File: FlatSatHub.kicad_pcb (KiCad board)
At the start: 2 copper layers, 129.3 x 129.3 mm, 24 parts, among them J1 DB26_Male_HighDensity_Mountin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, J10 Conn_02x02_Odd_Even, J11 DB26_Male_HighDensity_Mountin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, J12 Conn_02x02_Odd_Even, J13 DB26_Male_HighDensity_Mountin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, J14 Conn_02x02_Odd_Even, J15 DB26_Male_HighDensity_Mountin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, J16 Conn_02x02_Odd_Even, J2 Conn_02x02_Odd_Even, J3 DB26_Male_HighDensity_Mountin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, J4 Conn_02x02_Odd_Even, J5 DB26_Male_HighDensity_Mountin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, J6 Conn_02x02_Odd_Even, J7 DB26_Male_HighDensity_Mountin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, J8 Conn_02x02_Odd_Even, J9 DB26_Male_HighDensity_Mountin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, SW1 SW_SPST, SW2 SW_SPST, SW3 SW_SPST, SW4 SW_SPST, SW5 SW_SPST, SW6 SW_SPST, SW7 SW_SPST, SW8 SW_SPST

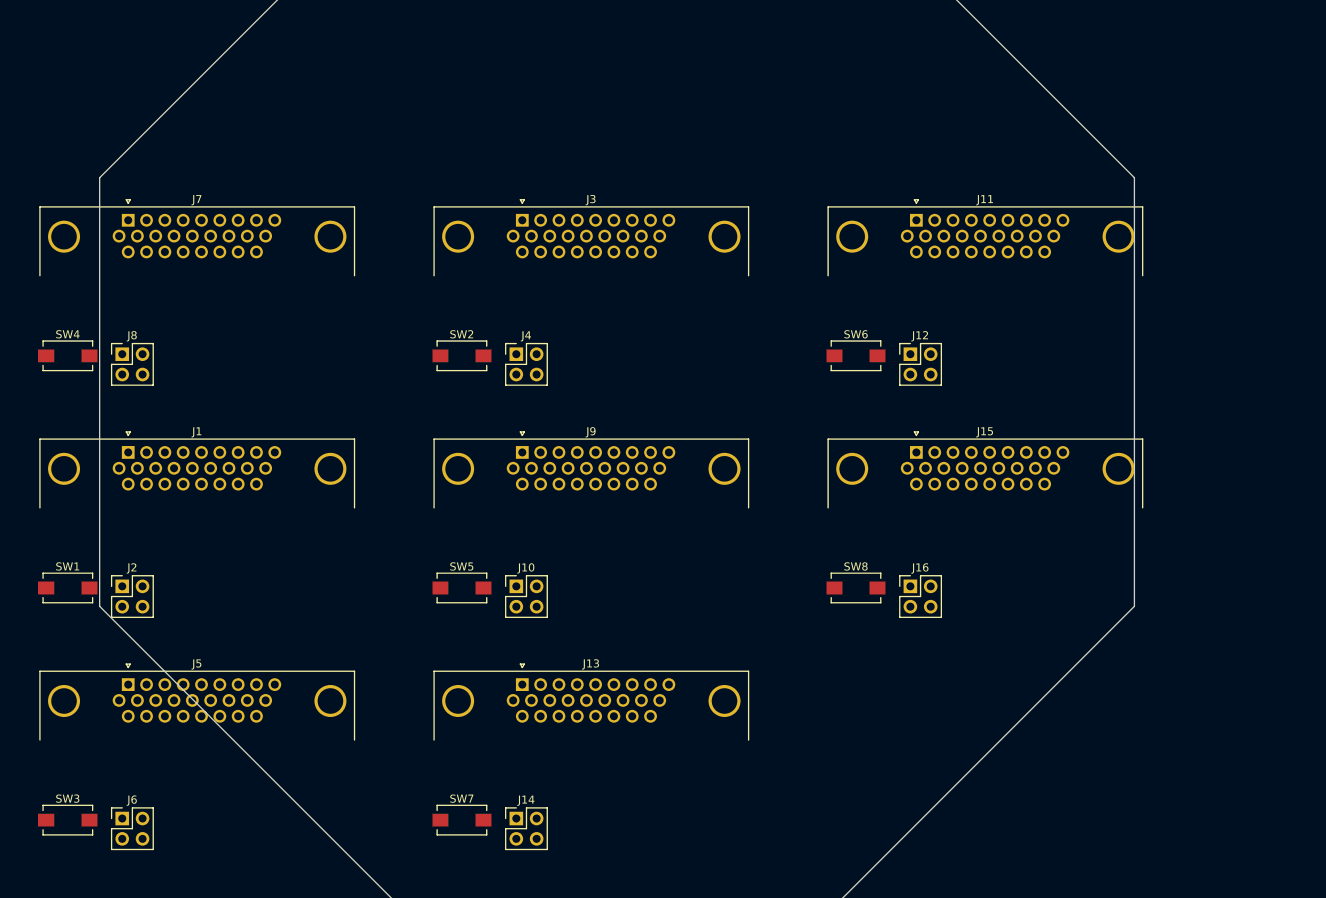
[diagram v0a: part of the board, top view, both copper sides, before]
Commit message: create footprints
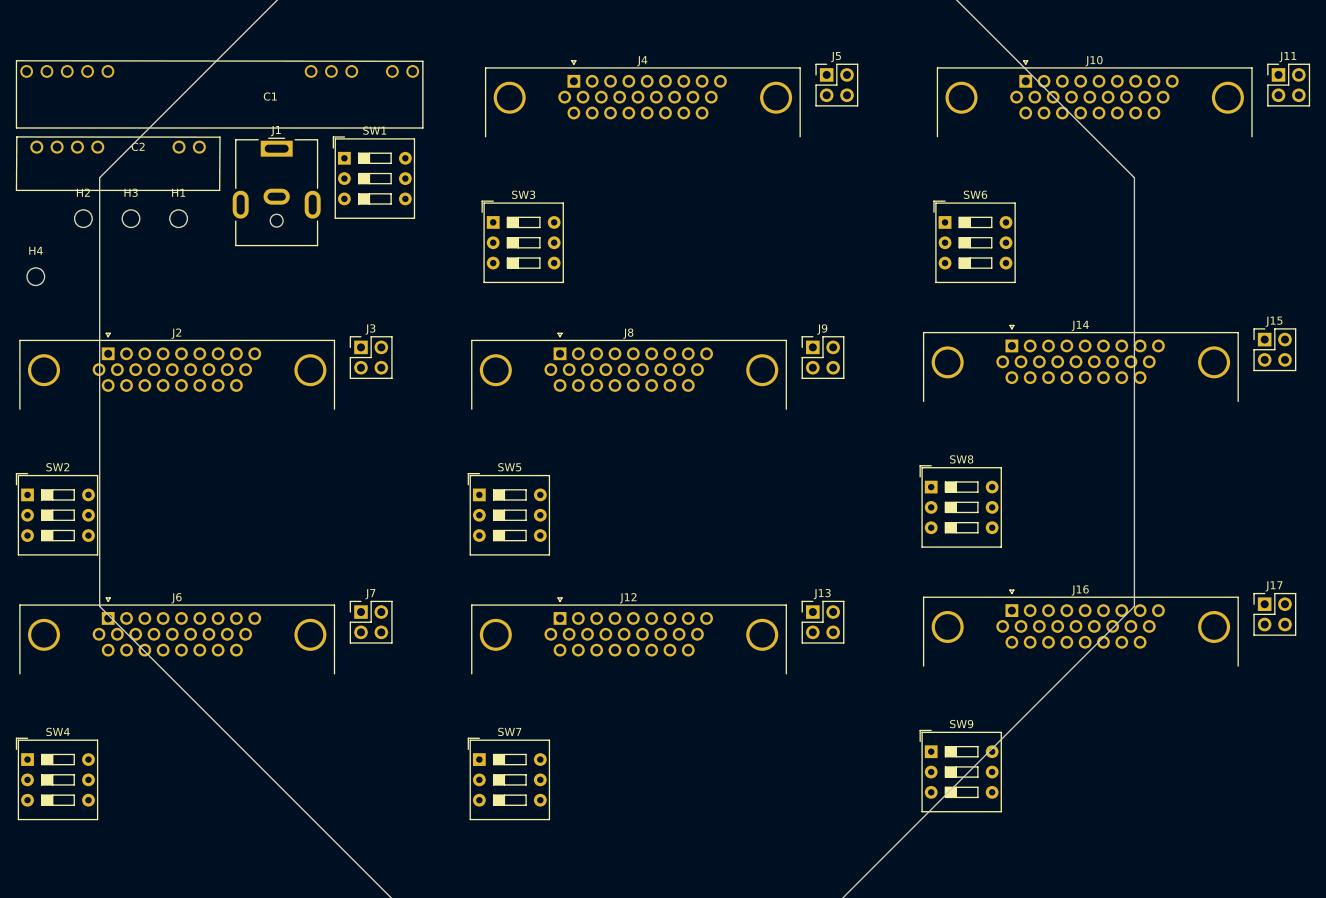
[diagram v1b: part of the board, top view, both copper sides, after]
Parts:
- added C1: CINCON-SIPSMT10-12, FlatSatHub:CINCON-SIPSMT10-12, F.Cu at (106.7, 34.9)
- added C2: bel-xRBA-06E2Ax, FlatSatHub:BEL-xRBA-06E2Ax, F.Cu at (87.6, 45.0)
- added H1: MountingHole_Pad, MountingHole:MountingHole_2.2mm_M2, F.Cu at (95.2, 53.3)
- added H2: MountingHole_Pad, MountingHole:MountingHole_2.2mm_M2, F.Cu at (83.3, 53.3)
- added H3: MountingHole_Pad, MountingHole:MountingHole_2.2mm_M2, F.Cu at (89.2, 53.3)
- added H4: MountingHole_Pad, MountingHole:MountingHole_2.2mm_M2, F.Cu at (77.3, 60.6)
- added J17: Conn_02x02_Odd_Even, Connector_PinHeader_2.54mm:PinHeader_2x02_P2.54mm_Vertical, F.Cu at (231.0, 101.5)
- added SW9: SW_DIP_x03, Button_Switch_THT:SW_DIP_SPSTx03_Slide_9.78x9.8mm_W7.62mm_P2.54mm, F.Cu at (189.3, 120.0)
- J1: value DB26_Male_HighDensity_MountingHoles -> Jack-DC; footprint Connector_Dsub:DSUB-26-HD_Male_Horizontal_P2.29x1.98mm_EdgePinOffset3.03mm_Housed_MountingHolesOffset4.94mm -> Connector_BarrelJack:BarrelJack_CUI_PJ-063AH_Horizontal
- J10, J12, J14, J16, J2, J4, J6, J8: value Conn_02x02_Odd_Even -> DB26_Male_HighDensity_MountingHoles; footprint Connector_PinHeader_2.54mm:PinHeader_2x02_P2.54mm_Vertical -> Connector_Dsub:DSUB-26-HD_Male_Horizontal_P2.29x1.98mm_EdgePinOffset3.03mm_Housed_MountingHolesOffset4.94mm
- J11, J13, J15, J3, J5, J7, J9: value DB26_Male_HighDensity_MountingHoles -> Conn_02x02_Odd_Even; footprint Connector_Dsub:DSUB-26-HD_Male_Horizontal_P2.29x1.98mm_EdgePinOffset3.03mm_Housed_MountingHolesOffset4.94mm -> Connector_PinHeader_2.54mm:PinHeader_2x02_P2.54mm_Vertical
- SW1, SW2, SW3, SW4, SW5, SW6, SW7, SW8: value SW_SPST -> SW_DIP_x03; footprint Button_Switch_SMD:SW_SPST_EVQPE1 -> Button_Switch_THT:SW_DIP_SPSTx03_Slide_9.78x9.8mm_W7.62mm_P2.54mm
- moved J5 115.9 mm to (176.2, 35.4)
- moved SW3 91.7 mm to (134.5, 53.8)
- moved J10 89.7 mm to (201.1, 36.2)
- moved J14 85.6 mm to (199.4, 69.2)
- moved SW1 63.9 mm to (115.9, 45.8)
- moved SW2 57.0 mm to (76.3, 87.9)
- moved J7 57.0 mm to (118.0, 102.5)
- moved J12 54.9 mm to (142.9, 103.3)
- moved J8 54.7 mm to (142.9, 70.2)
- moved SW4 50.7 mm to (76.3, 120.9)
- moved J11 48.8 mm to (232.7, 35.4)
- moved J15 45.8 mm to (231.0, 68.4)
- moved J1 42.3 mm to (107.5, 44.6)
- moved J9 38.6 mm to (174.5, 69.4)
- moved J13 37.4 mm to (174.5, 102.5)
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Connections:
- J1 pad 1: /sheet5F162098/I2C2_SDA -> /VBat
- J1 pad 2: /SPI1_MISO -> GND
- J10 pad 1: /sheet5F164939/UART2_TX -> I2C2_SDA
- J10 pad 2: /sheet5F164939/UART2_RX -> SPI1_MISO
- J10 pad 3: /sheet5F164939/UART1_TX -> SPI1_SS
- J10 pad 4: /sheet5F164939/UART1_RX -> SPI4_SS
- J11 pad 1: /sheet5F16493A/I2C2_SDA -> /sheet5F112855/sheet5F10EEC4/UART2_TX
- J11 pad 2: /SPI1_MISO -> /sheet5F112855/sheet5F10EEC4/UART2_RX
- J11 pad 3: /SPI1_SS -> /sheet5F112855/sheet5F10EEC4/UART1_TX
- J11 pad 4: /SPI4_SS -> /sheet5F112855/sheet5F10EEC4/UART1_RX
- J12 pad 1: /sheet5F16493A/UART2_TX -> I2C2_SDA
- J12 pad 2: /sheet5F16493A/UART2_RX -> SPI1_MISO
- J12 pad 3: /sheet5F16493A/UART1_TX -> SPI1_SS
- J12 pad 4: /sheet5F16493A/UART1_RX -> SPI4_SS
- J13 pad 1: /sheet5F16493B/I2C2_SDA -> /sheet5F112856/sheet5F10EEC4/UART2_TX
- J13 pad 2: /SPI1_MISO -> /sheet5F112856/sheet5F10EEC4/UART2_RX
- J13 pad 3: /SPI1_SS -> /sheet5F112856/sheet5F10EEC4/UART1_TX
- J13 pad 4: /SPI4_SS -> /sheet5F112856/sheet5F10EEC4/UART1_RX
- J14 pad 1: /sheet5F16493B/UART2_TX -> I2C2_SDA
- J14 pad 2: /sheet5F16493B/UART2_RX -> SPI1_MISO
- J14 pad 3: /sheet5F16493B/UART1_TX -> SPI1_SS
- J14 pad 4: /sheet5F16493B/UART1_RX -> SPI4_SS
- J15 pad 1: /sheet5F16493C/I2C2_SDA -> /sheet5F112857/sheet5F10EEC4/UART2_TX
- J15 pad 2: /SPI1_MISO -> /sheet5F112857/sheet5F10EEC4/UART2_RX
- J15 pad 3: /SPI1_SS -> /sheet5F112857/sheet5F10EEC4/UART1_TX
- J15 pad 4: /SPI4_SS -> /sheet5F112857/sheet5F10EEC4/UART1_RX
- J16 pad 1: /sheet5F16493C/UART2_TX -> I2C2_SDA
- J16 pad 2: /sheet5F16493C/UART2_RX -> SPI1_MISO
- J16 pad 3: /sheet5F16493C/UART1_TX -> SPI1_SS
- J16 pad 4: /sheet5F16493C/UART1_RX -> SPI4_SS
- J2 pad 1: /sheet5F162098/UART2_TX -> I2C2_SDA
- J2 pad 2: /sheet5F162098/UART2_RX -> SPI1_MISO
- J2 pad 3: /sheet5F162098/UART1_TX -> SPI1_SS
- J2 pad 4: /sheet5F162098/UART1_RX -> SPI4_SS
- J3 pad 1: /sheet5F162B0B/I2C2_SDA -> /Sheet5F10DACD/sheet5F10EEC4/UART2_TX
- J3 pad 2: /SPI1_MISO -> /Sheet5F10DACD/sheet5F10EEC4/UART2_RX
- J3 pad 3: /SPI1_SS -> /Sheet5F10DACD/sheet5F10EEC4/UART1_TX
- J3 pad 4: /SPI4_SS -> /Sheet5F10DACD/sheet5F10EEC4/UART1_RX
- J4 pad 1: /sheet5F162B0B/UART2_TX -> I2C2_SDA
- J4 pad 2: /sheet5F162B0B/UART2_RX -> SPI1_MISO
- J4 pad 3: /sheet5F162B0B/UART1_TX -> SPI1_SS
- J4 pad 4: /sheet5F162B0B/UART1_RX -> SPI4_SS
- J5 pad 1: /sheet5F162B0C/I2C2_SDA -> /sheet5F1123F7/sheet5F10EEC4/UART2_TX
- J5 pad 2: /SPI1_MISO -> /sheet5F1123F7/sheet5F10EEC4/UART2_RX
- J5 pad 3: /SPI1_SS -> /sheet5F1123F7/sheet5F10EEC4/UART1_TX
- J5 pad 4: /SPI4_SS -> /sheet5F1123F7/sheet5F10EEC4/UART1_RX
- J6 pad 1: /sheet5F162B0C/UART2_TX -> I2C2_SDA
- J6 pad 2: /sheet5F162B0C/UART2_RX -> SPI1_MISO
- J6 pad 3: /sheet5F162B0C/UART1_TX -> SPI1_SS
- J6 pad 4: /sheet5F162B0C/UART1_RX -> SPI4_SS
- J7 pad 1: /sheet5F15D03F/I2C2_SDA -> /sheet5F112649/sheet5F10EEC4/UART2_TX
- J7 pad 2: /SPI1_MISO -> /sheet5F112649/sheet5F10EEC4/UART2_RX
- J7 pad 3: /SPI1_SS -> /sheet5F112649/sheet5F10EEC4/UART1_TX
- J7 pad 4: /SPI4_SS -> /sheet5F112649/sheet5F10EEC4/UART1_RX
- J8 pad 1: /sheet5F15D03F/UART2_TX -> I2C2_SDA
- J8 pad 2: /sheet5F15D03F/UART2_RX -> SPI1_MISO
- J8 pad 3: /sheet5F15D03F/UART1_TX -> SPI1_SS
- J8 pad 4: /sheet5F15D03F/UART1_RX -> SPI4_SS
- J9 pad 1: /sheet5F164939/I2C2_SDA -> /sheet5F11264A/sheet5F10EEC4/UART2_TX
- J9 pad 2: /SPI1_MISO -> /sheet5F11264A/sheet5F10EEC4/UART2_RX
- J9 pad 3: /SPI1_SS -> /sheet5F11264A/sheet5F10EEC4/UART1_TX
- J9 pad 4: /SPI4_SS -> /sheet5F11264A/sheet5F10EEC4/UART1_RX
- SW1 pad 1: /VCC -> /VBat
- SW1 pad 2: /VCC -> /VBat
- SW2 pad 1: /VCC -> VCC
- SW2 pad 2: /VCC -> /Sheet5F10DACD/sheet5F10EEC4/3V3
- SW3 pad 1: /VCC -> VCC
- SW3 pad 2: /VCC -> /sheet5F1123F7/sheet5F10EEC4/3V3
- SW4 pad 1: /VCC -> VCC
- SW4 pad 2: /VCC -> /sheet5F112649/sheet5F10EEC4/3V3
- SW5 pad 1: /VCC -> VCC
- SW5 pad 2: /VCC -> /sheet5F11264A/sheet5F10EEC4/3V3
- SW6 pad 1: /VCC -> VCC
- SW6 pad 2: /VCC -> /sheet5F112855/sheet5F10EEC4/3V3
- SW7 pad 1: /VCC -> VCC
- SW7 pad 2: /VCC -> /sheet5F112856/sheet5F10EEC4/3V3
- SW8 pad 1: /VCC -> VCC
- SW8 pad 2: /VCC -> /sheet5F112857/sheet5F10EEC4/3V3

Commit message: First placement and autorouting
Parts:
- C1: value CINCON-SIPSMT10-12 -> SIPSMT10-12
- H1, H2, H3, H4: footprint MountingHole:MountingHole_2.2mm_M2 -> MountingHole:MountingHole_2.2mm_M2_Pad
- J10, J12, J14, J16, J2, J4, J6, J8: footprint Connector_Dsub:DSUB-26-HD_Male_Horizontal_P2.29x1.98mm_EdgePinOffset3.03mm_Housed_MountingHolesOffset4.94mm -> Connector_Dsub:DSUB-26-HD_Female_Horizontal_P2.29x1.98mm_EdgePinOffset8.35mm_Housed_MountingHolesOffset10.89mm
- moved H2 95.3 mm to (154.9, 116.2)
- moved H3 80.3 mm to (161.3, 88.9)
- moved J11 74.5 mm to (163.2, 62.2), turned to 135 degrees
- moved J9 71.2 mm to (103.5, 63.5), turned to 225 degrees
- moved C2 70.4 mm to (144.1, 87.0), turned to 270 degrees
- moved J1 68.7 mm to (134.0, 108.0), turned to 90 degrees
- moved J17 67.8 mm to (165.2, 118.2), turned to 45 degrees
- moved J15 60.2 mm to (174.6, 89.5), turned to 90 degrees
- moved J13 52.8 mm to (132.1, 134.0)
- moved J8 52.3 mm to (91.4, 61.0), turned to 225 degrees
- moved C1 49.6 mm to (120.7, 82.5), turned to 90 degrees
- moved J5 46.9 mm to (131.4, 49.5), turned to 180 degrees
- moved H4 43.0 mm to (108.6, 90.2)
- moved J12 40.2 mm to (142.9, 143.5)
- moved J10 39.0 mm to (163.8, 47.6), turned to 135 degrees
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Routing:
- net SPI4_MOSI: track 0.00 -> 397.0 mm, vias 0 -> 3
- net SPI4_MISO: track 0.00 -> 388.1 mm, vias 0 -> 4
- net SPI1_SS: track 0.00 -> 363.7 mm, vias 0 -> 4
- net SPI1_SCK: track 0.00 -> 360.9 mm, vias 0 -> 3
- net SPI4_SCK: track 0.00 -> 351.2 mm, vias 0 -> 5
- net CAN1_RX: track 0.00 -> 345.4 mm, vias 0 -> 4
- net I2C2_SCL: track 0.00 -> 343.6 mm, vias 0 -> 3
- net I2C1_SCL: track 0.00 -> 343.6 mm, vias 0 -> 3
- net I2C1_SDA: track 0.00 -> 342.3 mm, vias 0 -> 5
- net SPI1_MOSI: track 0.00 -> 340.0 mm, vias 0 -> 3
- net I2C2_SDA: track 0.00 -> 313.1 mm, vias 0 -> 4
- net CAN1_TX: track 0.00 -> 307.1 mm, vias 0 -> 4
- net SPI4_SS: track 0.00 -> 307.0 mm, vias 0 -> 3
- net SPI1_MISO: track 0.00 -> 306.8 mm, vias 0 -> 4
- net GND: track 0.00 -> 70.7 mm, vias 0 -> 3
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- added copper zone on In2.Cu, net /3V3
- added copper zone on B.Cu, net /5V
- added copper zone on F.Cu, net GND
- added copper zone on In1.Cu, net VCC
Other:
- copper layers 2 -> 4
- rule trace_min: 0.2 -> 0.15

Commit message: rework power management schematic
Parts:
- added R1: R, Resistor_SMD:R_0603_1608Metric_Pad1.05x0.95mm_HandSolder, F.Cu at (135.3, 101.0)
- added R2: R, Resistor_SMD:R_0603_1608Metric_Pad1.05x0.95mm_HandSolder, F.Cu at (137.8, 94.6)
- C1: value SIPSMT10-12 -> CINCON-SIPSMT10-12
- J10, J12, J14, J16, J2, J4, J6, J8: footprint Connector_Dsub:DSUB-26-HD_Female_Horizontal_P2.29x1.98mm_EdgePinOffset8.35mm_Housed_MountingHolesOffset10.89mm -> Connector_Dsub:DSUB-26-HD_Male_Horizontal_P2.29x1.98mm_EdgePinOffset3.03mm_Housed_MountingHolesOffset4.94mm
- moved J13 263.3 mm to (371.3, 24.0)
- moved J7 230.0 mm to (314.8, 24.0), turned to 0 degrees
- moved J12 229.8 mm to (339.7, 24.8)
- moved J17 214.9 mm to (371.3, 57.0), turned to 0 degrees
- moved J6 210.3 mm to (283.2, 24.8), turned to 0 degrees
- moved SW7 210.0 mm to (329.6, 42.4)
- moved SW4 187.7 mm to (273.1, 42.4), turned to 0 degrees
- moved SW9 181.1 mm to (329.6, 75.5), turned to 0 degrees
- moved J3 179.6 mm to (258.3, 24.0), turned to 0 degrees
- moved J16 175.3 mm to (339.7, 57.8), turned to 0 degrees
- moved J2 163.3 mm to (226.7, 24.8), turned to 0 degrees
- moved J9 157.1 mm to (258.3, 90.1), turned to 0 degrees
- moved J11 151.7 mm to (314.8, 57.0), turned to 0 degrees
- moved J15 140.2 mm to (314.8, 90.1), turned to 0 degrees
- moved J8 138.5 mm to (226.7, 90.9), turned to 0 degrees
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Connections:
- net /Sheet5F10DACD/sheet5F10EEC4/UART1_RX renamed /sheet5F1F8E85/UART1_RX
- net /Sheet5F10DACD/sheet5F10EEC4/UART1_TX renamed /sheet5F1F8E85/UART1_TX
- net /Sheet5F10DACD/sheet5F10EEC4/UART2_RX renamed /sheet5F1F8E85/UART2_RX
- net /Sheet5F10DACD/sheet5F10EEC4/UART2_TX renamed /sheet5F1F8E85/UART2_TX
- net /Sheet5F10DACD/sheet5F10EEC4/bus_3v3 renamed /sheet5F1F8E85/bus_3v3
- net /Sheet5F10DACD/sheet5F10EEC4/bus_5v renamed /sheet5F1F8E85/bus_5v
- net /Sheet5F10DACD/sheet5F10EEC4/bus_vbat renamed /sheet5F1F8E85/bus_vbat
- net /VBat renamed Net-(J1-Pad1)
- net /sheet5F1123F7/sheet5F10EEC4/UART1_RX renamed /sheet5F22A1B0/UART1_RX
- net /sheet5F1123F7/sheet5F10EEC4/UART1_TX renamed /sheet5F22A1B0/UART1_TX
- net /sheet5F1123F7/sheet5F10EEC4/UART2_RX renamed /sheet5F22A1B0/UART2_RX
- net /sheet5F1123F7/sheet5F10EEC4/UART2_TX renamed /sheet5F22A1B0/UART2_TX
- net /sheet5F1123F7/sheet5F10EEC4/bus_3v3 renamed /sheet5F22A1B0/bus_3v3
- net /sheet5F1123F7/sheet5F10EEC4/bus_5v renamed /sheet5F22A1B0/bus_5v
- net /sheet5F1123F7/sheet5F10EEC4/bus_vbat renamed /sheet5F22A1B0/bus_vbat
- net /sheet5F112649/sheet5F10EEC4/UART1_RX renamed /sheet5F22D1E8/UART1_RX
- net /sheet5F112649/sheet5F10EEC4/UART1_TX renamed /sheet5F22D1E8/UART1_TX
- net /sheet5F112649/sheet5F10EEC4/UART2_RX renamed /sheet5F22D1E8/UART2_RX
- net /sheet5F112649/sheet5F10EEC4/UART2_TX renamed /sheet5F22D1E8/UART2_TX
- net /sheet5F112649/sheet5F10EEC4/bus_3v3 renamed /sheet5F22D1E8/bus_3v3
- net /sheet5F112649/sheet5F10EEC4/bus_5v renamed /sheet5F22D1E8/bus_5v
- net /sheet5F112649/sheet5F10EEC4/bus_vbat renamed /sheet5F22D1E8/bus_vbat
- net /sheet5F11264A/sheet5F10EEC4/UART1_RX renamed /sheet5F22D1E9/UART1_RX
- net /sheet5F11264A/sheet5F10EEC4/UART1_TX renamed /sheet5F22D1E9/UART1_TX
- net /sheet5F11264A/sheet5F10EEC4/UART2_RX renamed /sheet5F22D1E9/UART2_RX
- net /sheet5F11264A/sheet5F10EEC4/UART2_TX renamed /sheet5F22D1E9/UART2_TX
- net /sheet5F11264A/sheet5F10EEC4/bus_3v3 renamed /sheet5F22D1E9/bus_3v3
- net /sheet5F11264A/sheet5F10EEC4/bus_5v renamed /sheet5F22D1E9/bus_5v
- net /sheet5F11264A/sheet5F10EEC4/bus_vbat renamed /sheet5F22D1E9/bus_vbat
- net /sheet5F112855/sheet5F10EEC4/UART1_RX renamed /sheet5F23178F/UART1_RX
- net /sheet5F112855/sheet5F10EEC4/UART1_TX renamed /sheet5F23178F/UART1_TX
- net /sheet5F112855/sheet5F10EEC4/UART2_RX renamed /sheet5F23178F/UART2_RX
- net /sheet5F112855/sheet5F10EEC4/UART2_TX renamed /sheet5F23178F/UART2_TX
- net /sheet5F112855/sheet5F10EEC4/bus_3v3 renamed /sheet5F23178F/bus_3v3
- net /sheet5F112855/sheet5F10EEC4/bus_5v renamed /sheet5F23178F/bus_5v
- net /sheet5F112855/sheet5F10EEC4/bus_vbat renamed /sheet5F23178F/bus_vbat
- net /sheet5F112856/sheet5F10EEC4/UART1_RX renamed /sheet5F231790/UART1_RX
- net /sheet5F112856/sheet5F10EEC4/UART1_TX renamed /sheet5F231790/UART1_TX
- net /sheet5F112856/sheet5F10EEC4/UART2_RX renamed /sheet5F231790/UART2_RX
- net /sheet5F112856/sheet5F10EEC4/UART2_TX renamed /sheet5F231790/UART2_TX
- net /sheet5F112856/sheet5F10EEC4/bus_3v3 renamed /sheet5F231790/bus_3v3
- net /sheet5F112856/sheet5F10EEC4/bus_5v renamed /sheet5F231790/bus_5v
- net /sheet5F112856/sheet5F10EEC4/bus_vbat renamed /sheet5F231790/bus_vbat
- net /sheet5F112857/sheet5F10EEC4/UART1_RX renamed /sheet5F237BCE/UART1_RX
- net /sheet5F112857/sheet5F10EEC4/UART1_TX renamed /sheet5F237BCE/UART1_TX
- net /sheet5F112857/sheet5F10EEC4/UART2_RX renamed /sheet5F237BCE/UART2_RX
- net /sheet5F112857/sheet5F10EEC4/UART2_TX renamed /sheet5F237BCE/UART2_TX
- net /sheet5F112857/sheet5F10EEC4/bus_3v3 renamed /sheet5F237BCE/bus_3v3
- net /sheet5F112857/sheet5F10EEC4/bus_5v renamed /sheet5F237BCE/bus_5v
- net /sheet5F112857/sheet5F10EEC4/bus_vbat renamed /sheet5F237BCE/bus_vbat
- net /sheet5F112858/sheet5F10EEC4/UART1_RX renamed /sheet5F237BCF/UART1_RX
- net /sheet5F112858/sheet5F10EEC4/UART1_TX renamed /sheet5F237BCF/UART1_TX
- net /sheet5F112858/sheet5F10EEC4/UART2_RX renamed /sheet5F237BCF/UART2_RX
- net /sheet5F112858/sheet5F10EEC4/UART2_TX renamed /sheet5F237BCF/UART2_TX
- net /sheet5F112858/sheet5F10EEC4/bus_3v3 renamed /sheet5F237BCF/bus_3v3
- net /sheet5F112858/sheet5F10EEC4/bus_5v renamed /sheet5F237BCF/bus_5v
- net /sheet5F112858/sheet5F10EEC4/bus_vbat renamed /sheet5F237BCF/bus_vbat
- net CAN1_RX renamed /CAN1_RX
- net CAN1_TX renamed /CAN1_TX
- net I2C1_SCL renamed /I2C1_SCL
- net I2C1_SDA renamed /I2C1_SDA
- net I2C2_SCL renamed /I2C2_SCL
- net I2C2_SDA renamed /I2C2_SDA
- net SPI1_MISO renamed /SPI1_MISO
- net SPI1_MOSI renamed /SPI1_MOSI
- net SPI1_SCK renamed /SPI1_SCK
- net SPI1_SS renamed /SPI1_SS
- net SPI4_MISO renamed /SPI4_MISO
- net SPI4_MOSI renamed /SPI4_MOSI
- net SPI4_SCK renamed /SPI4_SCK
- net SPI4_SS renamed /SPI4_SS
- net VCC renamed Vbat
- C1 pad 1: /3V3 -> 3V3
- C1 pad 11: /3V3-C-SW -> /PSU_3V3_ENABLE
- C1 pad 2: /3V3 -> 3V3
- C1 pad 4: /3V3 -> 3V3
- C2 pad 1: /5V -> 5V
- C2 pad 6: /5V-C-SW -> /PSU_5V_ENABLE
- SW1 pad 4: /3V3-C-SW -> /PSU_5V_ENABLE
- SW1 pad 5: /5V-C-SW -> /PSU_3V3_ENABLE
- SW2 pad 2: /Sheet5F10DACD/sheet5F10EEC4/3V3 -> 3V3
- SW2 pad 3: /Sheet5F10DACD/sheet5F10EEC4/5V -> 5V
- SW3 pad 2: /sheet5F1123F7/sheet5F10EEC4/3V3 -> 3V3
- SW3 pad 3: /sheet5F1123F7/sheet5F10EEC4/5V -> 5V
- SW4 pad 2: /sheet5F112649/sheet5F10EEC4/3V3 -> 3V3
- SW4 pad 3: /sheet5F112649/sheet5F10EEC4/5V -> 5V
- SW5 pad 2: /sheet5F11264A/sheet5F10EEC4/3V3 -> 3V3
- SW5 pad 3: /sheet5F11264A/sheet5F10EEC4/5V -> 5V
- SW6 pad 2: /sheet5F112855/sheet5F10EEC4/3V3 -> 3V3
- SW6 pad 3: /sheet5F112855/sheet5F10EEC4/5V -> 5V
- SW7 pad 2: /sheet5F112856/sheet5F10EEC4/3V3 -> 3V3
- SW7 pad 3: /sheet5F112856/sheet5F10EEC4/5V -> 5V
- SW8 pad 2: /sheet5F112857/sheet5F10EEC4/3V3 -> 3V3
- SW8 pad 3: /sheet5F112857/sheet5F10EEC4/5V -> 5V
- SW9 pad 2: /sheet5F112858/sheet5F10EEC4/3V3 -> 3V3
- SW9 pad 3: /sheet5F112858/sheet5F10EEC4/5V -> 5V
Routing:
- net /SPI4_MOSI: track 397.0 -> 0.00 mm, vias 3 -> 0
- net /SPI4_MISO: track 388.1 -> 0.00 mm, vias 4 -> 0
- net /SPI1_SS: track 363.7 -> 0.00 mm, vias 4 -> 0
- net /SPI1_SCK: track 360.9 -> 0.00 mm, vias 3 -> 0
- net /SPI4_SCK: track 351.2 -> 0.00 mm, vias 5 -> 0
- net /CAN1_RX: track 345.4 -> 0.00 mm, vias 4 -> 0
- net /I2C2_SCL: track 343.6 -> 0.00 mm, vias 3 -> 0
- net /I2C1_SCL: track 343.6 -> 0.00 mm, vias 3 -> 0
- net /I2C1_SDA: track 342.3 -> 0.00 mm, vias 5 -> 0
- net /SPI1_MOSI: track 340.0 -> 0.00 mm, vias 3 -> 0
- net /I2C2_SDA: track 313.1 -> 0.00 mm, vias 4 -> 0
- net /CAN1_TX: track 307.1 -> 0.00 mm, vias 4 -> 0
- net /SPI4_SS: track 307.0 -> 0.00 mm, vias 3 -> 0
- net /SPI1_MISO: track 306.8 -> 0.00 mm, vias 4 -> 0
- net GND: track 70.7 -> 0.00 mm, vias 3 -> 0
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- added copper zone on In1.Cu, net VCC
- removed copper zone on In1.Cu, net Vbat

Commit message: try improving positionning
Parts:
- removed R1, R2: R, Resistor_SMD:R_0603_1608Metric_Pad1.05x0.95mm_HandSolder
- added SW10: SW_SPDT, Button_Switch_SMD:SW_SPDT_PCM12, F.Cu at (83.8, 131.4)
- added SW11: SW_SPDT, Button_Switch_SMD:SW_SPDT_PCM12, F.Cu at (103.2, 131.4)
- J10, J12, J14, J16, J2, J4, J6, J8: footprint Connector_Dsub:DSUB-26-HD_Male_Horizontal_P2.29x1.98mm_EdgePinOffset3.03mm_Housed_MountingHolesOffset4.94mm -> DB-HD-26:DSUB-26-HD_Male_Horizontal_P2.29x1.98mm_EdgePinOffset3.03mm_Housed_MountingHolesOffset4.94mm_custom
- SW1: value SW_DIP_x03 -> SW_SPDT; footprint Button_Switch_THT:SW_DIP_SPSTx03_Slide_9.78x9.8mm_W7.62mm_P2.54mm -> Button_Switch_SMD:SW_SPDT_PCM12
- moved J12 285.6 mm to (94.8, 171.7)
- moved J11 283.6 mm to (34.8, 101.7), turned to 90 degrees
- moved J13 277.1 mm to (94.8, 41.6)
- moved J15 267.9 mm to (52.3, 144.1), turned to 135 degrees
- moved J7 264.8 mm to (52.3, 59.2), turned to 45 degrees
- moved J16 246.3 mm to (94.8, 31.6), turned to 180 degrees
- moved J10 238.0 mm to (45.3, 52.2), turned to 225 degrees
- moved SW9 235.2 mm to (94.8, 61.6)
- moved J17 234.1 mm to (137.2, 59.2), turned to 315 degrees
- moved SW7 208.8 mm to (123.0, 73.4), turned to 135 degrees
- moved SW8 207.7 mm to (66.5, 129.9), turned to 135 degrees
- moved J4 206.6 mm to (24.8, 101.7), turned to 270 degrees
- moved J8 191.2 mm to (45.3, 151.1), turned to 315 degrees
- moved SW6 190.2 mm to (94.8, 141.7), turned to 180 degrees
- moved J9 178.5 mm to (94.8, 161.7), turned to 180 degrees
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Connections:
- C1 pad 11: /PSU_3V3_ENABLE -> Net-(C1-Pad11)
- C1 pad 7: Vbat -> /Vin
- C1 pad 8: Vbat -> /Vin
- C2 pad 5: Vbat -> /Vin
- C2 pad 6: /PSU_5V_ENABLE -> Net-(C2-Pad6)
- J1 pad 1: Net-(J1-Pad1) -> /Vin
- SW1 pad 1: Net-(J1-Pad1) -> Vbat
- SW1 pad 2: Net-(J1-Pad1) -> /Vin
- SW1 pad 3: Net-(J1-Pad1) -> Net-(SW1-Pad3)
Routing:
- net Net-(J1-Pad1): track 43.2 -> 0.00 mm
- net /5V-C-SW: track 31.3 -> 0.00 mm
- net /3V3-C-SW: track 23.1 -> 0.00 mm
- added copper zone on In2.Cu, net 3V3
- added copper zone on B.Cu, net 5V
- removed copper zone on In2.Cu, net /3V3
- removed copper zone on B.Cu, net /5V
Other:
- board size 129.3 x 129.3 mm -> 147.8 x 147.8 mm

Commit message: re-place footprints for symmetry
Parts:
- moved J13 123.0 mm to (94.8, 164.7), turned to 180 degrees
- moved J5 123.0 mm to (31.8, 101.7)
- moved J15 87.0 mm to (139.3, 146.2), turned to 225 degrees
- moved J7 87.0 mm to (139.3, 57.1), turned to 315 degrees
- moved SW6 83.2 mm to (59.4, 66.3), turned to 45 degrees
- moved SW7 83.2 mm to (94.8, 151.7), turned to 180 degrees
- moved J1 70.8 mm to (165.2, 130.2)
- moved SW8 64.0 mm to (130.1, 137.0), turned to 225 degrees
- moved SW4 64.0 mm to (130.1, 66.3), turned to 315 degrees
- moved SW5 64.0 mm to (59.4, 137.0), turned to 135 degrees
- moved H2 48.5 mm to (77.5, 143.2)
- moved J11 47.2 mm to (50.2, 57.1), turned to 45 degrees
- moved J9 47.2 mm to (50.2, 146.2), turned to 135 degrees
- moved J17 47.2 mm to (94.8, 38.6), turned to 0 degrees
- moved J3 46.1 mm to (157.8, 101.7), turned to 270 degrees
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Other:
- board size 147.8 x 147.8 mm -> 166.3 x 166.3 mm
